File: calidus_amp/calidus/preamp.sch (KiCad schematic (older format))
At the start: 30 parts, among them U8 OPA2134

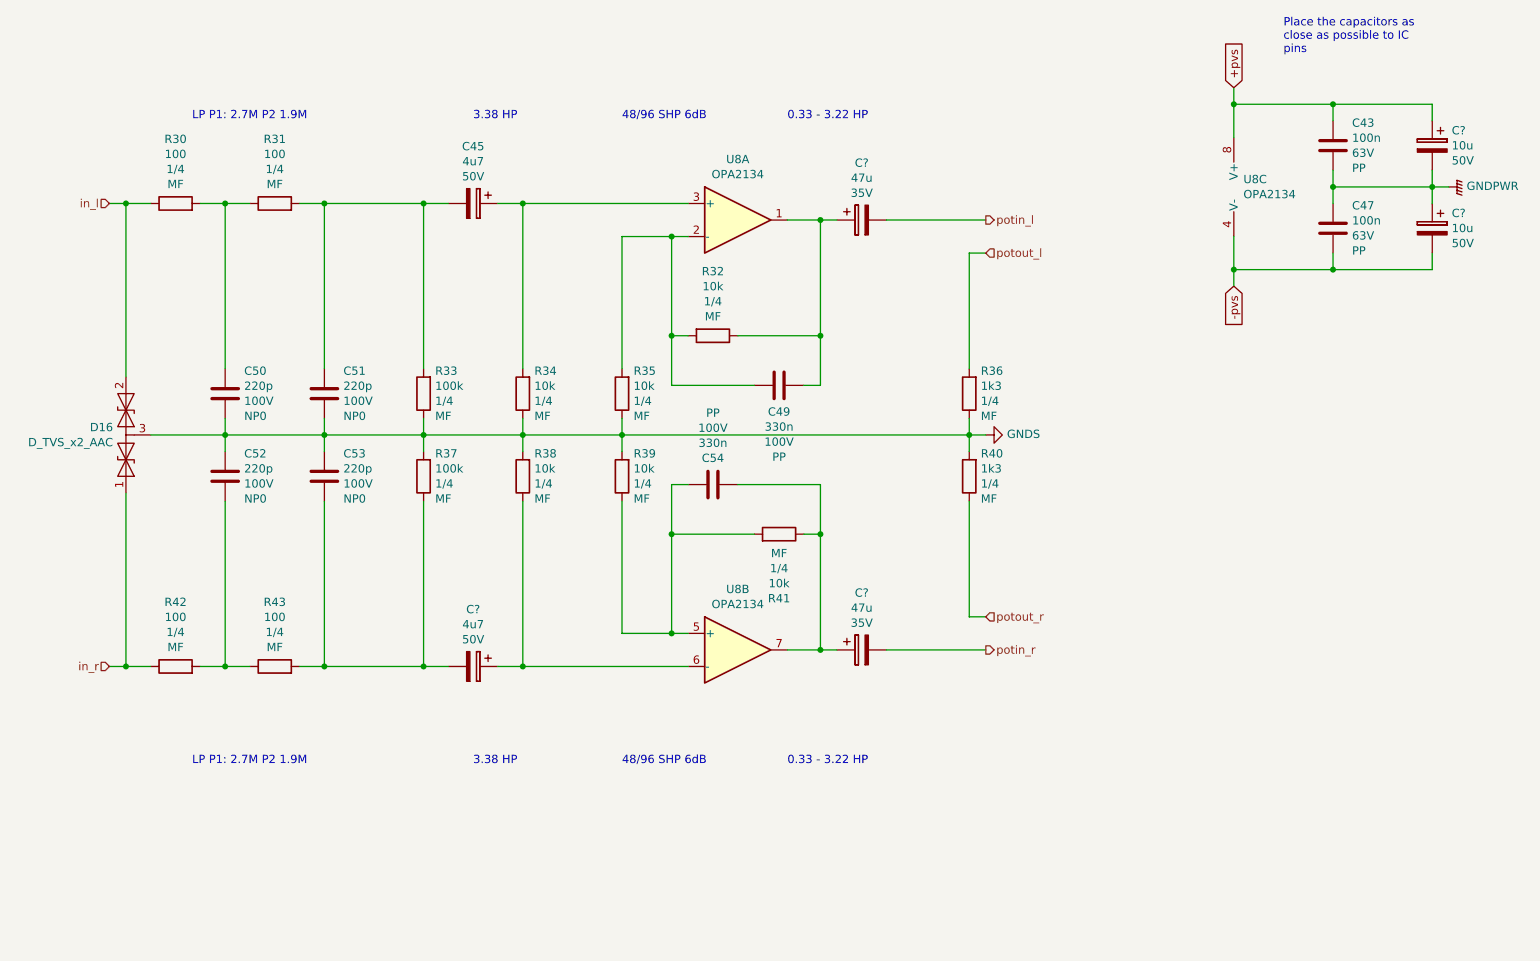
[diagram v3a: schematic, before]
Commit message: Annotated the schematic
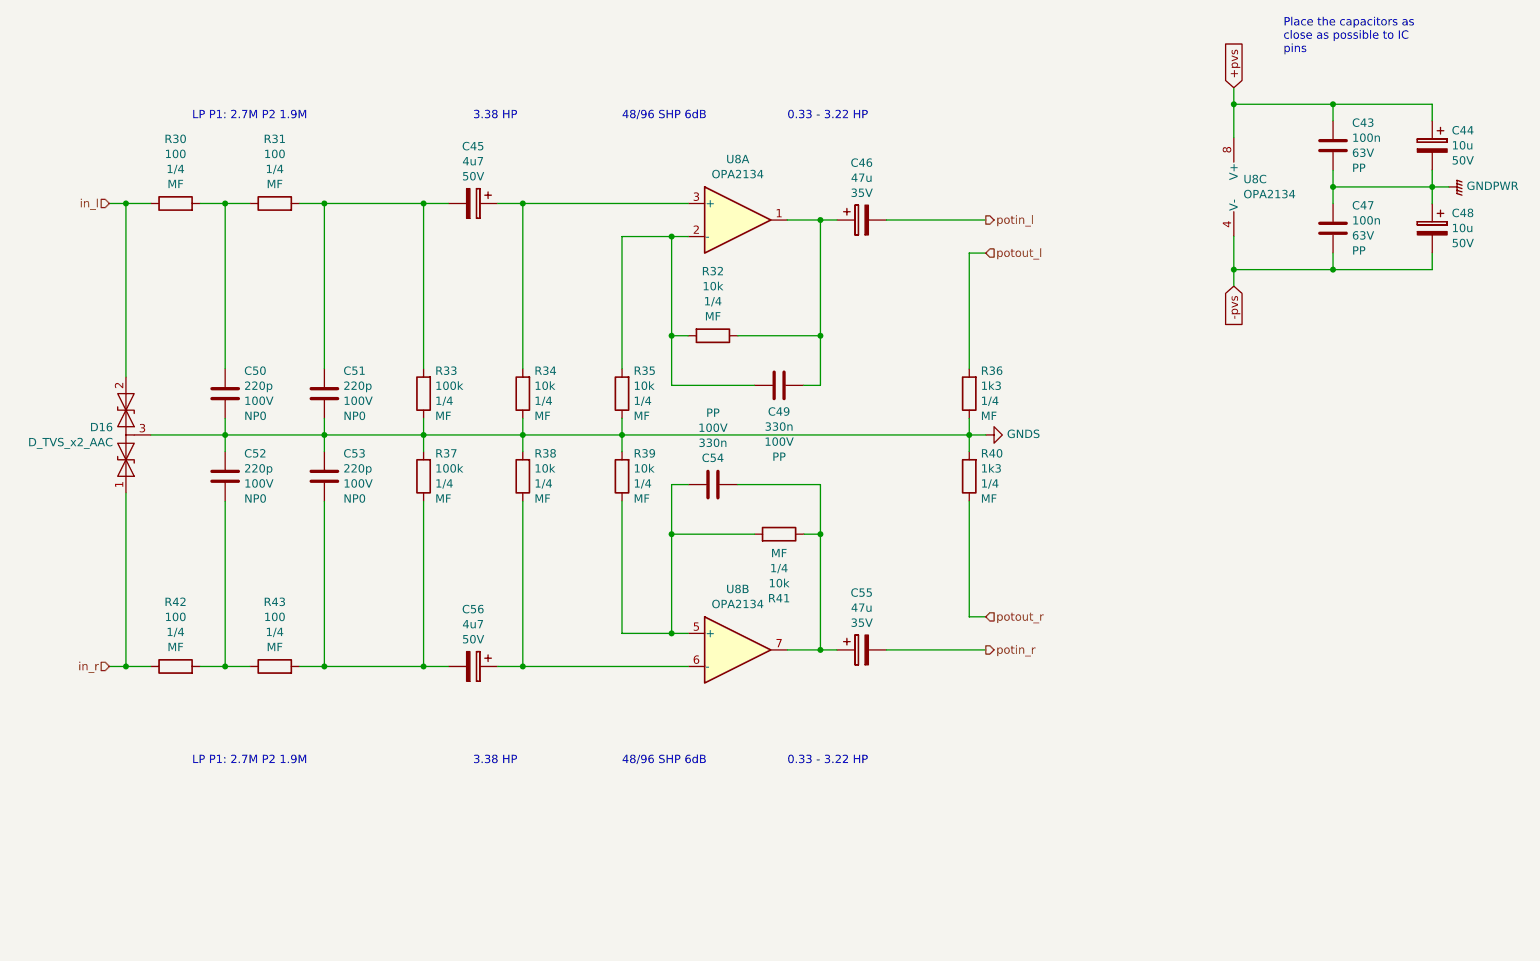
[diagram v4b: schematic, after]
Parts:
- gave numbers to parts that had none: 5
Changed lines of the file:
@@
 P 9800 2150
 AR Path="/5C37BC48/5C5A5B6F" Ref="C?"  Part="1"
-AR Path="/5C4751C0/5C5A5B6F" Ref="C?"  Part="1"
-F 0 "C?" H 9682 2241 50  0000 R CNN
+AR Path="/5C4751C0/5C5A5B6F" Ref="C44"  Part="1"
+F 0 "C44" H 9682 2241 50  0000 R CNN
 F 1 "10u" H 9682 2150 50  0000 R CNN
 F 2 "Capacitor_THT:CP_Radial_D5.0mm_P2.00mm" H 9838 2000 50  0001 C CNN
@@
 P 9800 2650
 AR Path="/5C37BC48/5C5A7F98" Ref="C?"  Part="1"
-AR Path="/5C4751C0/5C5A7F98" Ref="C?"  Part="1"
-F 0 "C?" H 9682 2741 50  0000 R CNN
+AR Path="/5C4751C0/5C5A7F98" Ref="C48"  Part="1"
+F 0 "C48" H 9682 2741 50  0000 R CNN
 F 1 "10u" H 9682 2650 50  0000 R CNN
 F 2 "Capacitor_THT:CP_Radial_D5.0mm_P2.00mm" H 9838 2500 50  0001 C CNN
@@
 $EndComp
 $Comp
-L Device:CP C?
+L Device:CP C56
 U 1 1 5C5AD364
 P 4000 5300
-F 0 "C?" V 3655 5300 50  0000 C CNN
+F 0 "C56" V 3655 5300 50  0000 C CNN
 F 1 "4u7" V 3746 5300 50  0000 C CNN
 F 2 "Capacitor_THT:CP_Radial_D5.0mm_P2.00mm" H 4038 5150 50  0001 C CNN
@@
 P 6350 2600
 AR Path="/5C37BC7C/5C5B02C7" Ref="C?"  Part="1"
-AR Path="/5C4751C0/5C5B02C7" Ref="C?"  Part="1"
-F 0 "C?" V 6005 2600 50  0000 C CNN
+AR Path="/5C4751C0/5C5B02C7" Ref="C46"  Part="1"
+F 0 "C46" V 6005 2600 50  0000 C CNN
 F 1 "47u" V 6096 2600 50  0000 C CNN
 F 2 "Capacitor_THT:CP_Radial_D6.3mm_P2.50mm" H 6388 2450 50  0001 C CNN
@@
 P 6350 5200
 AR Path="/5C37BC7C/5C5B28EB" Ref="C?"  Part="1"
-AR Path="/5C4751C0/5C5B28EB" Ref="C?"  Part="1"
-F 0 "C?" V 6005 5200 50  0000 C CNN
+AR Path="/5C4751C0/5C5B28EB" Ref="C55"  Part="1"
+F 0 "C55" V 6005 5200 50  0000 C CNN
 F 1 "47u" V 6096 5200 50  0000 C CNN
 F 2 "Capacitor_THT:CP_Radial_D6.3mm_P2.50mm" H 6388 5050 50  0001 C CNN

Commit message: WIP: Updated footprints
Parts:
- removed C45, C56: 4u7, Capacitor_THT:CP_Radial_D5.0mm_P2.00mm, symbol Device:CP
- removed C55: 47u, Capacitor_THT:CP_Radial_D6.3mm_P2.50mm, symbol Device:CP
- removed R32, R35, R38, R39, R41: 10k, symbol Device:R
- added C? (x2): 10u, Capacitor_THT:CP_Radial_D5.0mm_P2.00mm, symbol Device:CP
- added C?: 100u, Capacitor_THT:CP_Radial_D5.0mm_P2.50mm, symbol Device:CP
- added R? (x5): 12k, symbol Device:R
- C46: value 47u -> 100u; footprint Capacitor_THT:CP_Radial_D6.3mm_P2.50mm -> Capacitor_THT:CP_Radial_D5.0mm_P2.50mm; Manufacturer Rybicon:35YXF47MEFC6.3X11 -> Rybicon:10YXF100MEFC5X11; Supplier1 Farnell:1144626 -> Farnell:1144608; Voltage 35V -> 10V
- R34: value 10k -> 12k
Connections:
- net GNDS: now also R?.1, R?.2, R?.2
- net potin_r: now also C?.2
- net at C46.1, C49.1, U8.1: now also R?.2
- net at C49.2, U8.2 (-): now also R?.1, R?.2
- net at U8.6 (-): now also C?.1, R?.1
- net at C54.1, U8.7: now also C?.1, R?.2
- net at C54.2, U8.5 (+): now also R?.1, R?.1
- net at R34.2, U8.3 (+): now also C?.1
- net at C51.1, R31.2, R33.2: now also C?.2
- net at C53.2, R37.1, R43.2: now also C?.2
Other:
- note added: "1.32 HP"
- note added: "40/80 SHP 6dB"
- note removed: "3.38 HP"
- note removed: "48/96 SHP 6dB"
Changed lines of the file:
@@
 $EndDescr
-$Comp
-L Device:R R41
-U 1 1 5C47524D
-P 5850 4500
-F 0 "R41" V 5461 4500 50  0000 C CNN
-F 1 "10k" V 5552 4500 50  0000 C CNN
-F 2 "" V 5780 4500 50  0001 C CNN
-F 3 "~" H 5850 4500 50  0001 C CNN
-F 4 "1/4" V 5643 4500 50  0000 C CNN "Power"
-F 5 "MF" V 5734 4500 50  0000 C CNN "Type"
-	1    5850 4500
-	0    1    -1   0
-$EndComp
 $Comp
 L Device:R R34
@@
 P 4300 3650
 F 0 "R34" H 4230 3513 50  0000 R CNN
-F 1 "10k" H 4230 3604 50  0000 R CNN
+F 1 "12k" H 4230 3604 50  0000 R CNN
 F 2 "" V 4230 3650 50  0001 C CNN
 F 3 "~" H 4300 3650 50  0001 C CNN
@@
 	6100 4200 6100 4500
 Connection ~ 6100 4500
-$Comp
-L Device:CP C45
-U 1 1 5C4758D5
-P 4000 2500
-F 0 "C45" V 3655 2500 50  0000 C CNN
-F 1 "4u7" V 3746 2500 50  0000 C CNN
-F 2 "Capacitor_THT:CP_Radial_D5.0mm_P2.00mm" H 4038 2350 50  0001 C CNN
-F 3 "http://www.farnell.com/datasheets/2321304.pdf" H 4000 2500 50  0001 C CNN
-F 4 "50V" V 3837 2500 50  0000 C CNN "Voltage"
-F 5 "Rybicon:50YXF4R7MEFC5X11" V 4000 2500 50  0001 C CNN "Manufacturer"
-F 6 "Farnell:2811491" V 4000 2500 50  0001 C CNN "Supplier1"
-	1    4000 2500
-	0    1    1    0
-$EndComp
 Wire Wire Line
 	4150 2500 4300 2500
@@
 Wire Wire Line
 	5900 5200 6100 5200
-$Comp
-L Device:R R32
-U 1 1 5C41BC02
-P 5450 3300
-F 0 "R32" V 5061 3300 50  0000 C CNN
-F 1 "10k" V 5152 3300 50  0000 C CNN
-F 2 "" V 5380 3300 50  0001 C CNN
-F 3 "~" H 5450 3300 50  0001 C CNN
-F 4 "1/4" V 5243 3300 50  0000 C CNN "Power"
-F 5 "MF" V 5334 3300 50  0000 C CNN "Type"
-	1    5450 3300
-	0    1    1    0
-$EndComp
 Wire Wire Line
 	5300 3300 5200 3300
@@
 Wire Wire Line
 	4150 5300 4300 5300
-$Comp
-L Device:R R38
-U 1 1 5C421401
-P 4300 4150
-F 0 "R38" H 4230 4013 50  0000 R CNN
-F 1 "10k" H 4230 4104 50  0000 R CNN
-F 2 "" V 4230 4150 50  0001 C CNN
-F 3 "~" H 4300 4150 50  0001 C CNN
-F 4 "1/4" H 4230 4195 50  0000 R CNN "Power"
-F 5 "MF" H 4230 4286 50  0000 R CNN "Type"
-	1    4300 4150
-	-1   0    0    1
-$EndComp
 Wire Wire Line
 	4300 4300 4300 5300
@@
 Wire Wire Line
 	3100 5300 3700 5300
-$Comp
-L Device:R R35
-U 1 1 5C4B330E
-P 4900 3650
-F 0 "R35" H 4830 3513 50  0000 R CNN
-F 1 "10k" H 4830 3604 50  0000 R CNN
-F 2 "" V 4830 3650 50  0001 C CNN
-F 3 "~" H 4900 3650 50  0001 C CNN
-F 4 "1/4" H 4830 3695 50  0000 R CNN "Power"
-F 5 "MF" H 4830 3786 50  0000 R CNN "Type"
-	1    4900 3650
-	-1   0    0    1
-$EndComp
 Wire Wire Line
 	4900 3800 4900 3900
@@
 	4900 5100 5200 5100
 Connection ~ 5200 5100
-$Comp
-L Device:R R39
-U 1 1 5C4B70DD
-P 4900 4150
-F 0 "R39" H 4830 4013 50  0000 R CNN
-F 1 "10k" H 4830 4104 50  0000 R CNN
-F 2 "" V 4830 4150 50  0001 C CNN
-F 3 "~" H 4900 4150 50  0001 C CNN
-F 4 "1/4" H 4830 4195 50  0000 R CNN "Power"
-F 5 "MF" H 4830 4286 50  0000 R CNN "Type"
-	1    4900 4150
-	-1   0    0    1
-$EndComp
 Wire Wire Line
 	4900 4300 4900 5100
@@
 0.33 - 3.22 HP
 Text Notes 4900 5900 0    50   ~ 0
-48/96 SHP 6dB
+40/80 SHP 6dB
 Text Notes 4000 2000 0    50   ~ 0
-3.38 HP
+1.32 HP
 Text Notes 4900 2000 0    50   ~ 0
-48/96 SHP 6dB
+40/80 SHP 6dB
 Text Notes 5900 5900 0    50   ~ 0
 0.33 - 3.22 HP
 Text Notes 4000 5900 0    50   ~ 0
-3.38 HP
+1.32 HP
 Text Notes 2300 2000 0    50   ~ 0
 LP P1: 2.7M P2 1.9M
@@
 $EndComp
 $Comp
-L Device:CP C56
-U 1 1 5C5AD364
-P 4000 5300
-F 0 "C56" V 3655 5300 50  0000 C CNN
-F 1 "4u7" V 3746 5300 50  0000 C CNN
-F 2 "Capacitor_THT:CP_Radial_D5.0mm_P2.00mm" H 4038 5150 50  0001 C CNN
-F 3 "http://www.farnell.com/datasheets/2321304.pdf" H 4000 5300 50  0001 C CNN
-F 4 "50V" V 3837 5300 50  0000 C CNN "Voltage"
-F 5 "Rybicon:50YXF4R7MEFC5X11" V 4000 5300 50  0001 C CNN "Manufacturer"
-F 6 "Farnell:2811491" V 4000 5300 50  0001 C CNN "Supplier1"
-	1    4000 5300
-	0    1    1    0
-$EndComp
-$Comp
 L Device:CP C?
 U 1 1 5C5B02C7
@@
 AR Path="/5C4751C0/5C5B02C7" Ref="C46"  Part="1"
 F 0 "C46" V 6005 2600 50  0000 C CNN
-F 1 "47u" V 6096 2600 50  0000 C CNN
-F 2 "Capacitor_THT:CP_Radial_D6.3mm_P2.50mm" H 6388 2450 50  0001 C CNN
+F 1 "100u" V 6096 2600 50  0000 C CNN
+F 2 "Capacitor_THT:CP_Radial_D5.0mm_P2.50mm" H 6388 2450 50  0001 C CNN
 F 3 "http://www.farnell.com/datasheets/2321304.pdf" H 6350 2600 50  0001 C CNN
-F 4 "35V" V 6187 2600 50  0000 C CNN "Voltage"
-F 5 "Rybicon:35YXF47MEFC6.3X11" H 6350 2600 50  0001 C CNN "Manufacturer"
-F 6 "Farnell:1144626" H 6350 2600 50  0001 C CNN "Supplier1"
+F 4 "10V" V 6187 2600 50  0000 C CNN "Voltage"
+F 5 "Rybicon:10YXF100MEFC5X11" H 6350 2600 50  0001 C CNN "Manufacturer"
+F 6 "Farnell:1144608" H 6350 2600 50  0001 C CNN "Supplier1"
 	1    6350 2600
 	0    -1   1    0
@@
 $Comp
 L Device:CP C?
-U 1 1 5C5B28EB
+U 1 1 5C4DF67F
+P 4000 2500
+AR Path="/5C37BC48/5C4DF67F" Ref="C?"  Part="1"
+AR Path="/5C4751C0/5C4DF67F" Ref="C?"  Part="1"
+F 0 "C?" V 3655 2500 50  0000 C CNN
+F 1 "10u" V 3746 2500 50  0000 C CNN
+F 2 "Capacitor_THT:CP_Radial_D5.0mm_P2.00mm" H 4038 2350 50  0001 C CNN
+F 3 "http://www.farnell.com/datasheets/2124421.pdf" H 4000 2500 50  0001 C CNN
+F 4 "50V" V 3837 2500 50  0000 C CNN "Voltage"
+F 5 "Rybicon:50YXF10MEFC5X11" H 4000 2500 50  0001 C CNN "Manufacturer"
+F 6 "Farnell:1144632" H 4000 2500 50  0001 C CNN "Supplier1"
+	1    4000 2500
+	0    1    1    0
+$EndComp
+$Comp
+L Device:CP C?
+U 1 1 5C4E1C0C
+P 4000 5300
+AR Path="/5C37BC48/5C4E1C0C" Ref="C?"  Part="1"
+AR Path="/5C4751C0/5C4E1C0C" Ref="C?"  Part="1"
+F 0 "C?" V 3655 5300 50  0000 C CNN
+F 1 "10u" V 3746 5300 50  0000 C CNN
+F 2 "Capacitor_THT:CP_Radial_D5.0mm_P2.00mm" H 4038 5150 50  0001 C CNN
+F 3 "http://www.farnell.com/datasheets/2124421.pdf" H 4000 5300 50  0001 C CNN
+F 4 "50V" V 3837 5300 50  0000 C CNN "Voltage"
+F 5 "Rybicon:50YXF10MEFC5X11" H 4000 5300 50  0001 C CNN "Manufacturer"
+F 6 "Farnell:1144632" H 4000 5300 50  0001 C CNN "Supplier1"
+	1    4000 5300
+	0    1    1    0
+$EndComp
+$Comp
+L Device:R R?
+U 1 1 5C4EADDD
+P 4300 4150
+F 0 "R?" H 4230 4013 50  0000 R CNN
+F 1 "12k" H 4230 4104 50  0000 R CNN
+F 2 "" V 4230 4150 50  0001 C CNN
+F 3 "~" H 4300 4150 50  0001 C CNN
+F 4 "1/4" H 4230 4195 50  0000 R CNN "Power"
+F 5 "MF" H 4230 4286 50  0000 R CNN "Type"
+	1    4300 4150
+	-1   0    0    1
+$EndComp
+$Comp
+L Device:R R?
+U 1 1 5C4EAE35
+P 4900 3650
+F 0 "R?" H 4830 3513 50  0000 R CNN
+F 1 "12k" H 4830 3604 50  0000 R CNN
+F 2 "" V 4830 3650 50  0001 C CNN
+F 3 "~" H 4900 3650 50  0001 C CNN
+F 4 "1/4" H 4830 3695 50  0000 R CNN "Power"
+F 5 "MF" H 4830 3786 50  0000 R CNN "Type"
+	1    4900 3650
+	-1   0    0    1
+$EndComp
+$Comp
+L Device:R R?
+U 1 1 5C4EAE91
+P 4900 4150
+F 0 "R?" H 4830 4013 50  0000 R CNN
+F 1 "12k" H 4830 4104 50  0000 R CNN
+F 2 "" V 4830 4150 50  0001 C CNN
+F 3 "~" H 4900 4150 50  0001 C CNN
+F 4 "1/4" H 4830 4195 50  0000 R CNN "Power"
+F 5 "MF" H 4830 4286 50  0000 R CNN "Type"
+	1    4900 4150
+	-1   0    0    1
+$EndComp
+$Comp
+L Device:R R?
+U 1 1 5C4EAEE1
+P 5450 3300
+F 0 "R?" V 5839 3300 50  0000 C CNN
+F 1 "12k" V 5748 3300 50  0000 C CNN
+F 2 "" V 5380 3300 50  0001 C CNN
+F 3 "~" H 5450 3300 50  0001 C CNN
+F 4 "1/4" V 5657 3300 50  0000 C CNN "Power"
+F 5 "MF" V 5566 3300 50  0000 C CNN "Type"
+	1    5450 3300
+	0    -1   -1   0
+$EndComp
+$Comp
+L Device:R R?
+U 1 1 5C4EB04C
+P 5850 4500
+F 0 "R?" V 5735 4500 50  0000 C CNN
+F 1 "12k" V 5644 4500 50  0000 C CNN
+F 2 "" V 5780 4500 50  0001 C CNN
+F 3 "~" H 5850 4500 50  0001 C CNN
+F 4 "1/4" V 5553 4500 50  0000 C CNN "Power"
+F 5 "MF" V 5462 4500 50  0000 C CNN "Type"
+	1    5850 4500
+	0    -1   -1   0
+$EndComp
+$Comp
+L Device:CP C?
+U 1 1 5C4F4C34
 P 6350 5200
-AR Path="/5C37BC7C/5C5B28EB" Ref="C?"  Part="1"
-AR Path="/5C4751C0/5C5B28EB" Ref="C55"  Part="1"
-F 0 "C55" V 6005 5200 50  0000 C CNN
-F 1 "47u" V 6096 5200 50  0000 C CNN
-F 2 "Capacitor_THT:CP_Radial_D6.3mm_P2.50mm" H 6388 5050 50  0001 C CNN
+AR Path="/5C37BC7C/5C4F4C34" Ref="C?"  Part="1"
+AR Path="/5C4751C0/5C4F4C34" Ref="C?"  Part="1"
+F 0 "C?" V 6005 5200 50  0000 C CNN
+F 1 "100u" V 6096 5200 50  0000 C CNN
+F 2 "Capacitor_THT:CP_Radial_D5.0mm_P2.50mm" H 6388 5050 50  0001 C CNN
 F 3 "http://www.farnell.com/datasheets/2321304.pdf" H 6350 5200 50  0001 C CNN
-F 4 "35V" V 6187 5200 50  0000 C CNN "Voltage"
-F 5 "Rybicon:35YXF47MEFC6.3X11" H 6350 5200 50  0001 C CNN "Manufacturer"
-F 6 "Farnell:1144626" H 6350 5200 50  0001 C CNN "Supplier1"
+F 4 "10V" V 6187 5200 50  0000 C CNN "Voltage"
+F 5 "Rybicon:10YXF100MEFC5X11" H 6350 5200 50  0001 C CNN "Manufacturer"
+F 6 "Farnell:1144608" H 6350 5200 50  0001 C CNN "Supplier1"
 	1    6350 5200
 	0    -1   1    0
